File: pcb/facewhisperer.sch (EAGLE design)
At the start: 15 parts, among them IC1 XMEGA128D4, J1 CWTIO-20PIN, J2 VUSB IN, J3 USB-A-H, J5 CLK3, J6 RESET, U1 MAX3421ESMD, U2 NC7WZ14, X1 CLK1, X2 CLK2

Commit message: First rev of the PCB design
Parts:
- added C2, C3, C4, C5: 100n, SparkFun-Passives:CAP0805
- added C6: 1u, SparkFun-Passives:CAP0805
- added F1: PTC 2A, SparkFun-PowerIC:PTCSMD-W
- added H1, H2, H3, H4: MOUNT-HOLE3.2, holes:MOUNT-HOLE3.2
- added LED1: Power, adafruit:LEDSMT1206
- added LED2: Reset, adafruit:LEDSMT1206
- added LED3: VBUS, adafruit:LEDSMT1206
- added LED4: PA5, adafruit:LEDSMT1206
- added LED5: PA6, adafruit:LEDSMT1206
- added R10, R11, R4, R6, R7: 1k, SparkFun-Passives:RESISTOR0805-RES
- added R2, R5: 100, SparkFun-Passives:RESISTOR0805-RES
- added R3: 10k, SparkFun-Passives:RESISTOR0805-RES
- added R8, R9: 33, SparkFun-Passives:RESISTOR0805-RES
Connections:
- new net N$10: LED3.A, R7.1
- new net N$11: R9.2, U1.D-
- new net N$12: R8.2, U1.D+
- new net N$13: F1.1, J2.PWR
- new net N$14: LED4.A, R10.1
- new net N$15: LED5.A, R11.1
- new net N$16: IC1.PA6, LED5.C
- new net N$17: IC1.PA5, LED4.C
- new net N$4: R5.2, U1.X1
- new net N$6: LED2.A, R4.2
- new net N$7: IC1.PR1(XT1), R2.2
- new net N$9: LED1.A, R6.1
- new net PDI_CLK: IC1.!RESET!/PDI_CLK, J1.PDIC, R3.1
- new net PDI_DATA: IC1.PDI_DATA, J1.PDID
- new net TIO1: IC1.PC3, J1.FIO1
- new net TIO2: IC1.PC2, J1.FIO2
- new net TIO3: IC1.PA1, J1.FIO3
- new net TIO4: IC1.PA0, J1.FIO4
- new net USB_GPX: IC1.PC0, U1.GPX
- new net USB_IRQ: IC1.PB2, U1.INT
- new net USB_MISO: IC1.PC6, U1.MISO
- new net USB_MOSI: IC1.PC5, U1.MOSI
- new net USB_RESET: IC1.PC1, U1.RES
- new net USB_SCK: IC1.PC7, U1.SCK
- new net USB_SS: IC1.PC4, U1.SS
- net 3.3V: now also C2.1, C3.1, C4.1, C5.1, C6.1, IC1.AVCC, IC1.VCC, IC1.VCC1, IC1.VCC2, J1.VREF, R10.2, R11.2, R3.2, R6.2, U1.VCC, U1.VL
- net CLK12: now also J1.FHS2, R2.1, R5.1
- net D+: now also R8.1
- net D-: now also R9.1
- net GND: now also C2.2, C3.2, C4.2, C5.2, C6.2, J1.GND@0, J1.GND@1, J1.GND@2, LED1.C, LED2.C, LED3.C, U1.GND@19, U1.GND@3
- net N$5: now also F1.2, R7.2; no longer J2.PWR
- net RESET_GATE: now also IC1.PA7, R4.1
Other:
- note added: "scanlime"
- moved on the sheet: J1, J2, J4, J6, Q1, U1

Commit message: Rev A
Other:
- note added: "A"
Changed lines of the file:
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@@
 <plain>
 <text x="270.256" y="144.018" size="2.1844" layer="94" font="fixed">scanlime</text>
+<text x="338.836" y="141.478" size="2.1844" layer="94" font="fixed">A</text>
 </plain>
 <instances>

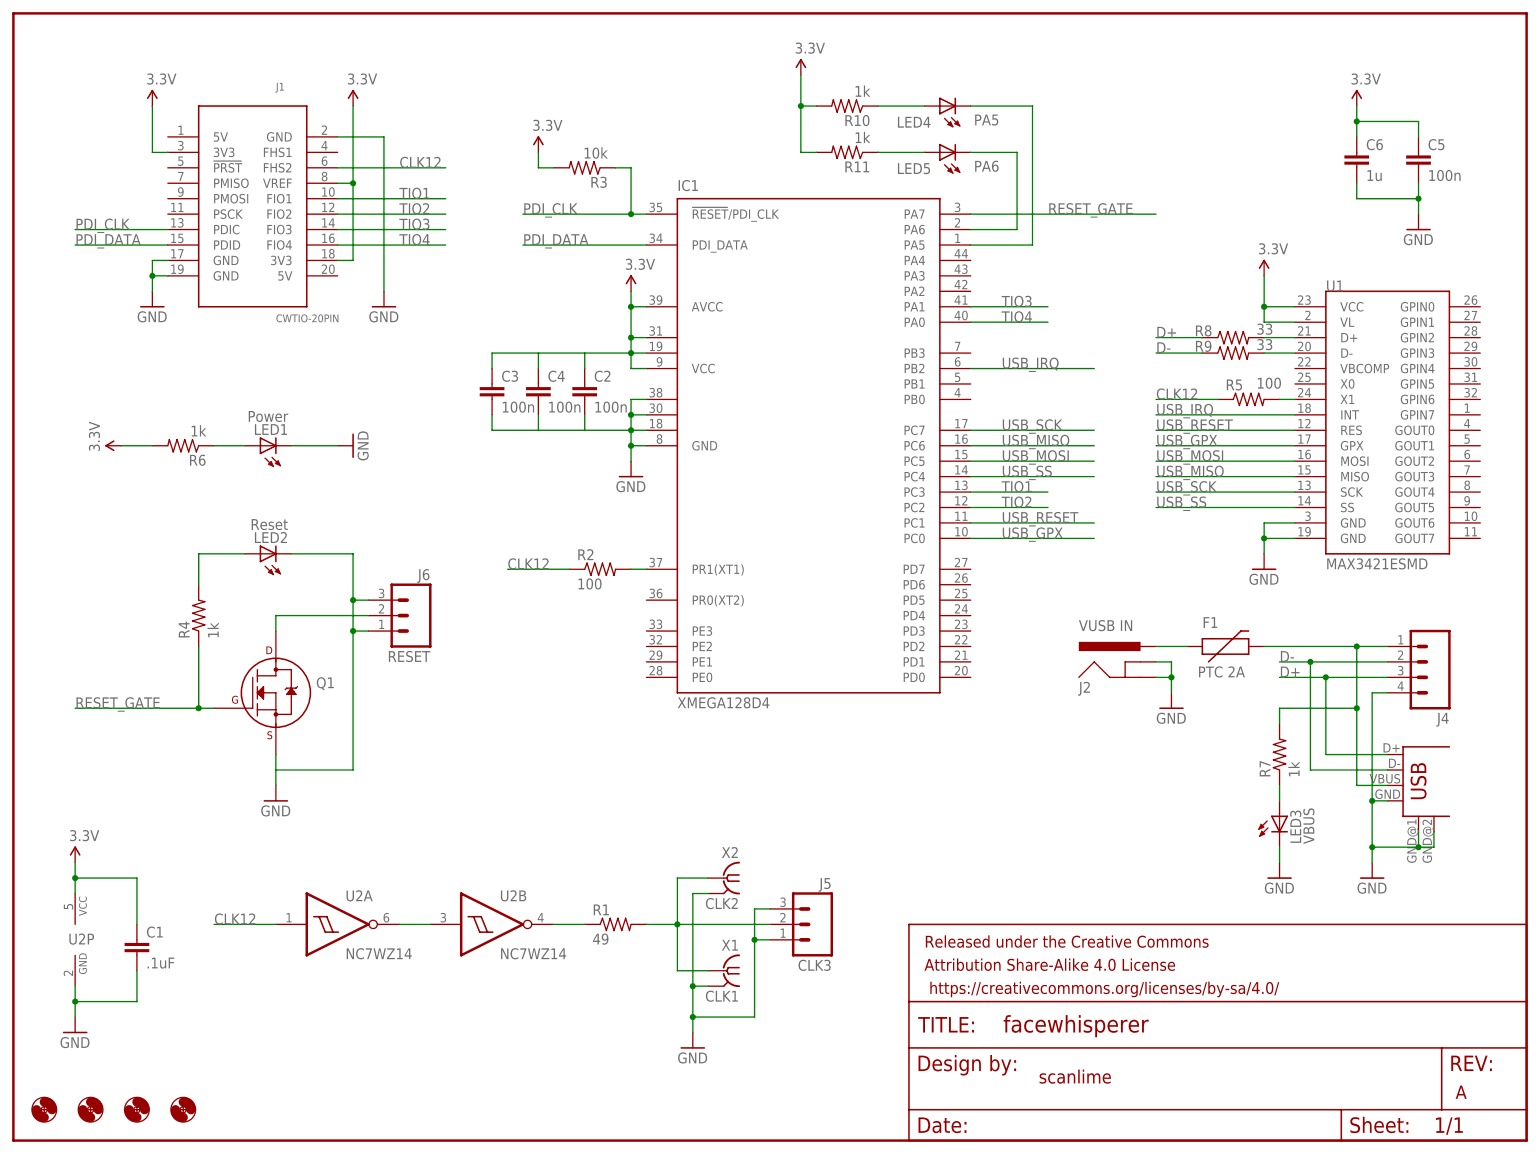
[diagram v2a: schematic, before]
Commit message: Add a sync input for use with analog comparator
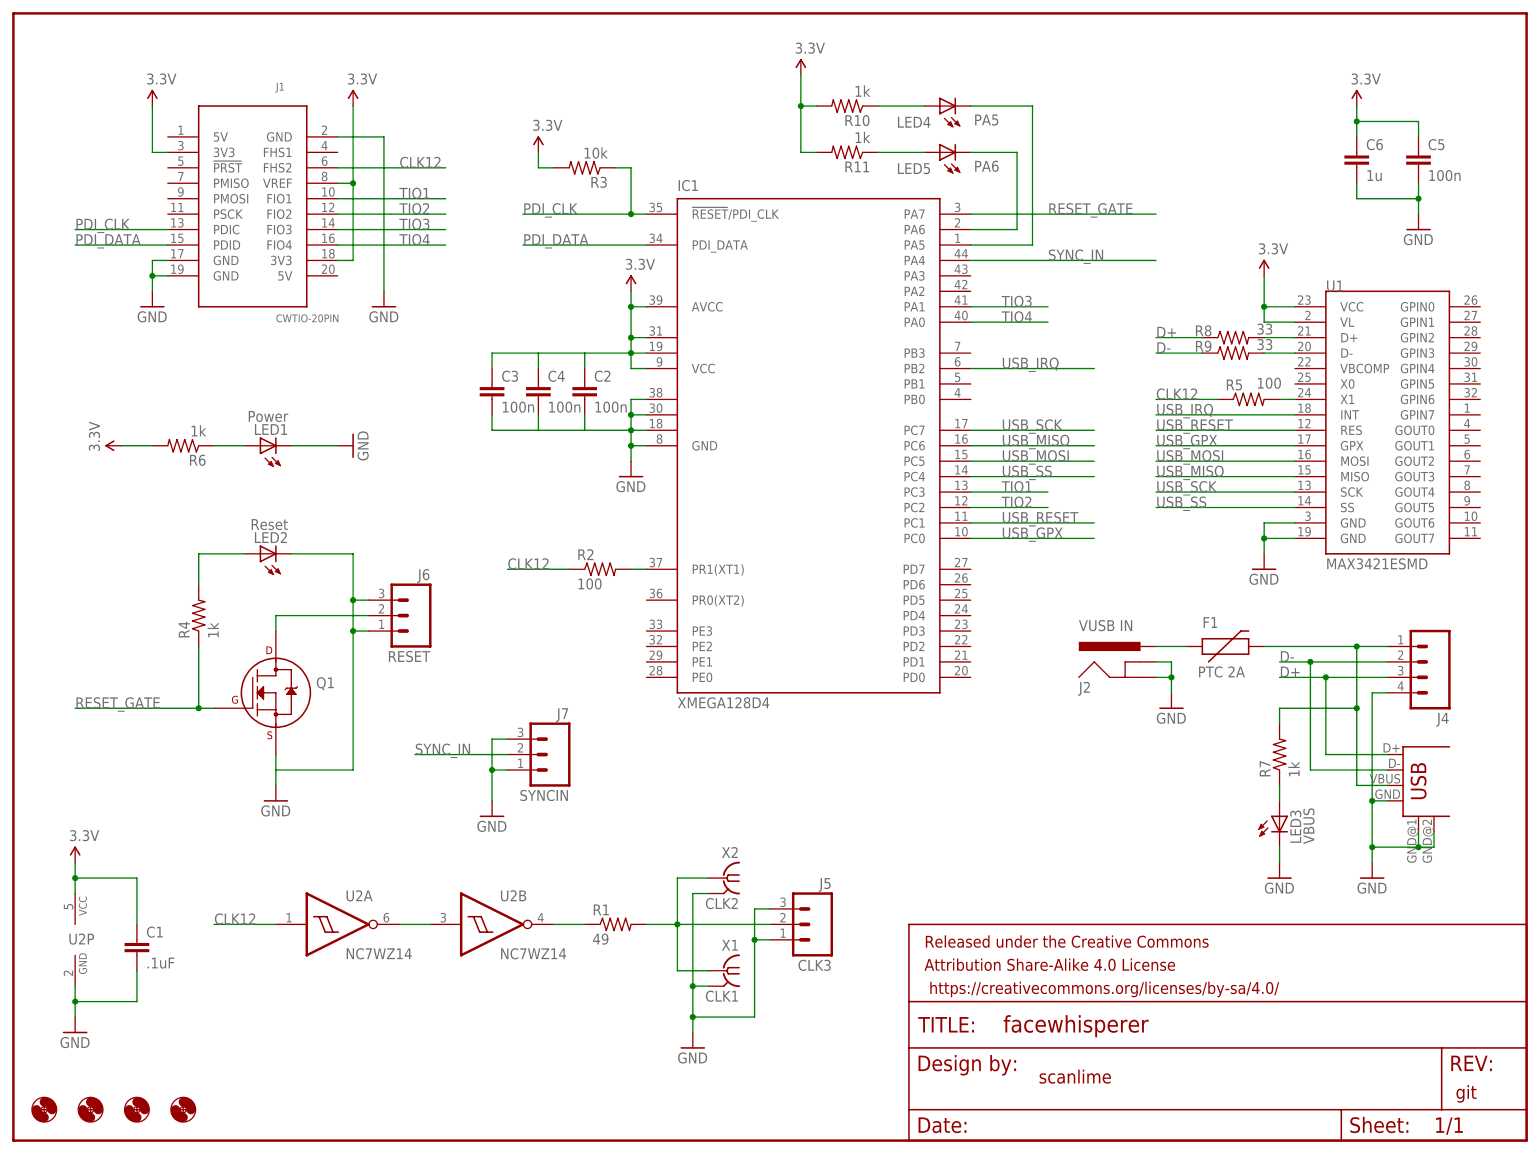
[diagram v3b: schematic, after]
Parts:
- added J7: SYNCIN, SparkFun-Connectors:M03LOCK_LONGPADS
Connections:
- new net SYNC_IN: IC1.PA4, J7.2
- net GND: now also J7.1, J7.3
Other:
- note added: "git"
- note removed: "A"
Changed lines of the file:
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@@
 <grid distance="0.1" unitdist="inch" unit="inch" style="lines" multiple="1" display="no" altdistance="0.01" altunitdist="inch" altunit="inch"/>
 <layers>
-<layer number="1" name="Top" color="4" fill="1" visible="yes" active="no"/>
-<layer number="16" name="Bottom" color="1" fill="1" visible="yes" active="no"/>
-<layer number="17" name="Pads" color="2" fill="1" visible="yes" active="no"/>
-<layer number="18" name="Vias" color="2" fill="1" visible="yes" active="no"/>
-<layer number="19" name="Unrouted" color="6" fill="1" visible="yes" active="no"/>
-<layer number="20" name="Dimension" color="15" fill="1" visible="yes" active="no"/>
-<layer number="21" name="tPlace" color="7" fill="1" visible="yes" active="no"/>
-<layer number="22" name="bPlace" color="7" fill="1" visible="yes" active="no"/>
-<layer number="23" name="tOrigins" color="15" fill="1" visible="yes" active="no"/>
-<layer number="24" name="bOrigins" color="15" fill="1" visible="yes" active="no"/>
-<layer number="25" name="tNames" color="7" fill="1" visible="yes" active="no"/>
-<layer number="26" name="bNames" color="7" fill="1" visible="yes" active="no"/>
-<layer number="27" name="tValues" color="7" fill="1" visible="yes" active="no"/>
-<layer number="28" name="bValues" color="7" fill="1" visible="yes" active="no"/>
+<layer number="1" name="Top" color="4" fill="1" visible="no" active="no"/>
+<layer number="16" name="Bottom" color="1" fill="1" visible="no" active="no"/>
+<layer number="17" name="Pads" color="2" fill="1" visible="no" active="no"/>
+<layer number="18" name="Vias" color="2" fill="1" visible="no" active="no"/>
+<layer number="19" name="Unrouted" color="6" fill="1" visible="no" active="no"/>
+<layer number="20" name="Dimension" color="15" fill="1" visible="no" active="no"/>
+<layer number="21" name="tPlace" color="7" fill="1" visible="no" active="no"/>
+<layer number="22" name="bPlace" color="7" fill="1" visible="no" active="no"/>
+<layer number="23" name="tOrigins" color="15" fill="1" visible="no" active="no"/>
+<layer number="24" name="bOrigins" color="15" fill="1" visible="no" active="no"/>
+<layer number="25" name="tNames" color="7" fill="1" visible="no" active="no"/>
+<layer number="26" name="bNames" color="7" fill="1" visible="no" active="no"/>
+<layer number="27" name="tValues" color="7" fill="1" visible="no" active="no"/>
+<layer number="28" name="bValues" color="7" fill="1" visible="no" active="no"/>
 <layer number="29" name="tStop" color="7" fill="3" visible="no" active="no"/>
 <layer number="30" name="bStop" color="7" fill="6" visible="no" active="no"/>
@@
 <layer number="35" name="tGlue" color="7" fill="4" visible="no" active="no"/>
 <layer number="36" name="bGlue" color="7" fill="5" visible="no" active="no"/>
-<layer number="37" name="tTest" color="7" fill="1" visible="yes" active="no"/>
-<layer number="38" name="bTest" color="7" fill="1" visible="yes" active="no"/>
+<layer number="37" name="tTest" color="7" fill="1" visible="no" active="no"/>
+<layer number="38" name="bTest" color="7" fill="1" visible="no" active="no"/>
 <layer number="39" name="tKeepout" color="4" fill="11" visible="no" active="no"/>
 <layer number="40" name="bKeepout" color="1" fill="11" visible="no" active="no"/>
@@
 <layer number="44" name="Drills" color="7" fill="1" visible="no" active="no"/>
 <layer number="45" name="Holes" color="7" fill="1" visible="no" active="no"/>
-<layer number="46" name="Milling" color="3" fill="1" visible="yes" active="no"/>
-<layer number="47" name="Measures" color="7" fill="1" visible="yes" active="no"/>
-<layer number="48" name="Document" color="7" fill="1" visible="yes" active="no"/>
-<layer number="49" name="Reference" color="7" fill="1" visible="yes" active="no"/>
-<layer number="50" name="dxf" color="7" fill="1" visible="yes" active="no"/>
-<layer number="51" name="tDocu" color="7" fill="1" visible="yes" active="no"/>
-<layer number="52" name="bDocu" color="7" fill="1" visible="yes" active="no"/>
-<layer number="53" name="tGND_GNDA" color="7" fill="9" visible="yes" active="no"/>
-<layer number="54" name="bGND_GNDA" color="1" fill="9" visible="yes" active="no"/>
-<layer number="56" name="wert" color="7" fill="1" visible="yes" active="no"/>
-<layer number="57" name="tCAD" color="7" fill="1" visible="yes" active="no"/>
-<layer number="59" name="tCarbon" color="7" fill="1" visible="yes" active="no"/>
-<layer number="60" name="bCarbon" color="7" fill="1" visible="yes" active="no"/>
+<layer number="46" name="Milling" color="3" fill="1" visible="no" active="no"/>
+<layer number="47" name="Measures" color="7" fill="1" visible="no" active="no"/>
+<layer number="48" name="Document" color="7" fill="1" visible="no" active="no"/>
+<layer number="49" name="Reference" color="7" fill="1" visible="no" active="no"/>
+<layer number="50" name="dxf" color="7" fill="1" visible="no" active="no"/>
+<layer number="51" name="tDocu" color="7" fill="1" visible="no" active="no"/>
+<layer number="52" name="bDocu" color="7" fill="1" visible="no" active="no"/>
+<layer number="53" name="tGND_GNDA" color="7" fill="9" visible="no" active="no"/>
+<layer number="54" name="bGND_GNDA" color="1" fill="9" visible="no" active="no"/>
+<layer number="56" name="wert" color="7" fill="1" visible="no" active="no"/>
+<layer number="57" name="tCAD" color="7" fill="1" visible="no" active="no"/>
+<layer number="59" name="tCarbon" color="7" fill="1" visible="no" active="no"/>
+<layer number="60" name="bCarbon" color="7" fill="1" visible="no" active="no"/>
 <layer number="90" name="Modules" color="5" fill="1" visible="yes" active="yes"/>
 <layer number="91" name="Nets" color="2" fill="1" visible="yes" active="yes"/>
@@
 <part name="GND12" library="SparkFun-Aesthetics" deviceset="GND" device=""/>
 <part name="GND13" library="SparkFun-Aesthetics" deviceset="GND" device=""/>
+<part name="J7" library="SparkFun-Connectors" deviceset="M03" device="LOCK_LONGPADS" value="SYNCIN"/>
+<part name="GND11" library="SparkFun-Aesthetics" deviceset="GND" device=""/>
 </parts>
 <sheets>
@@
 <plain>
 <text x="270.256" y="144.018" size="2.1844" layer="94" font="fixed">scanlime</text>
-<text x="338.836" y="141.478" size="2.1844" layer="94" font="fixed">A</text>
+<text x="338.836" y="141.478" size="2.1844" layer="94" font="fixed">git</text>
 </plain>
 <instances>
@@
 <instance part="GND12" gate="1" x="292.1" y="205.74"/>
 <instance part="GND13" gate="1" x="309.88" y="177.8"/>
+<instance part="J7" gate="J$1" x="190.5" y="198.12" rot="MR0"/>
+<instance part="GND11" gate="1" x="180.34" y="187.96"/>
 </instances>
 <busses>
@@
 <pinref part="GND13" gate="1" pin="GND"/>
 </segment>
+<segment>
+<pinref part="J7" gate="J$1" pin="3"/>
+<pinref part="GND11" gate="1" pin="GND"/>
+<wire x1="182.88" y1="200.66" x2="180.34" y2="200.66" width="0.1524" layer="91"/>
+<wire x1="180.34" y1="200.66" x2="180.34" y2="195.58" width="0.1524" layer="91"/>
+<pinref part="J7" gate="J$1" pin="1"/>
+<wire x1="180.34" y1="195.58" x2="180.34" y2="190.5" width="0.1524" layer="91"/>
+<wire x1="182.88" y1="195.58" x2="180.34" y2="195.58" width="0.1524" layer="91"/>
+<junction x="180.34" y="195.58"/>
+</segment>
 </net>
 <net name="3.3V" class="0">
@@
 </segment>
 </net>
+<net name="SYNC_IN" class="0">
+<segment>
+<pinref part="IC1" gate="G$1" pin="PA4"/>
+<wire x1="259.08" y1="279.4" x2="289.56" y2="279.4" width="0.1524" layer="91"/>
+<label x="271.78" y="279.4" size="1.778" layer="95"/>
+</segment>
+<segment>
+<pinref part="J7" gate="J$1" pin="2"/>
+<wire x1="182.88" y1="198.12" x2="167.64" y2="198.12" width="0.1524" layer="91"/>
+<label x="167.64" y="198.12" size="1.778" layer="95"/>
+</segment>
+</net>
